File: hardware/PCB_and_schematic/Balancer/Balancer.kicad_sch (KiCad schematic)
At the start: 0 parts

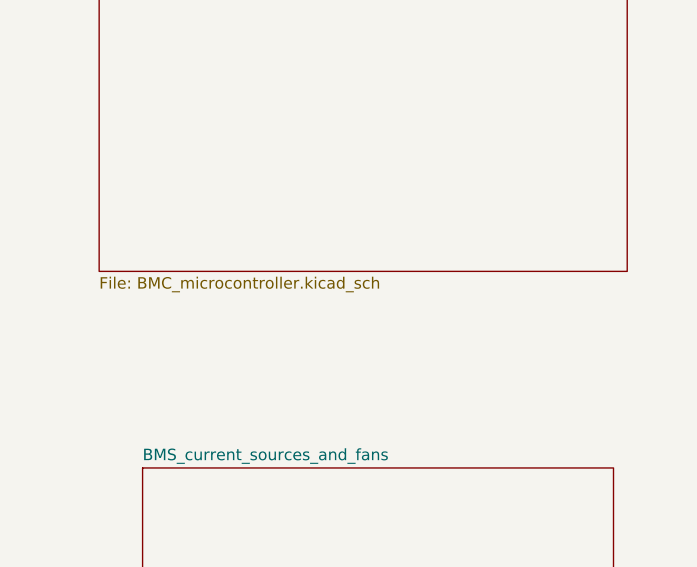
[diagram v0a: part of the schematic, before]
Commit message: Add simulations and recheck schematics + cleanup
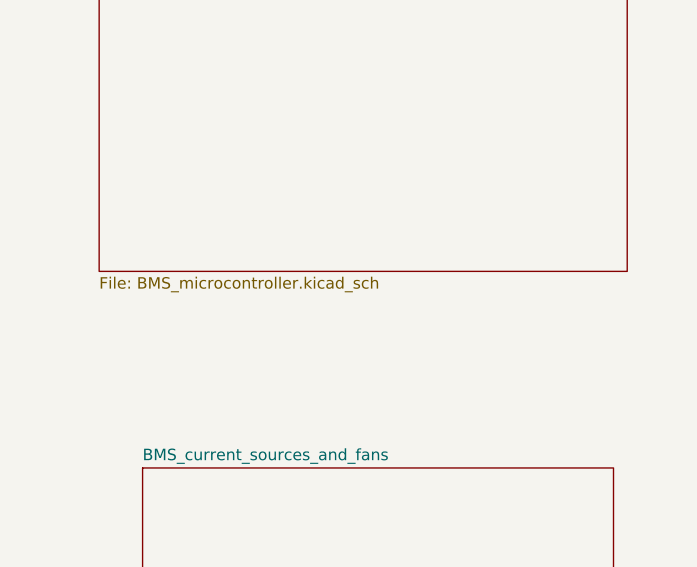
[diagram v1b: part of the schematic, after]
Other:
- sheet BMS_microcontroller: file BMC_microcontroller.kicad_sch -> BMS_microcontroller.kicad_sch
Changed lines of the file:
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@@
 			)
 		)
-		(property "Sheetfile" "BMC_microcontroller.kicad_sch"
+		(property "Sheetfile" "BMS_microcontroller.kicad_sch"
 			(at 68.834 105.7406 0)
 			(effects
